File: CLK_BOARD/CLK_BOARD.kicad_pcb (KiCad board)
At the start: 4 copper layers, 73.6 x 37.4 mm, 83 parts, among them J1 PWR, J2 OUT_50M_1, J3 OUT_50M_2, J4 OUT_50M_3, J5 OUT_50M_4, J6 OUT_100M_3, J7 OUT_100M_2, J8 OUT_100M_1, J9 Conn_01x04, U1 TPS7A9101DSKR, U2 LMK00804BQWRGTRQ1, U3 LMK00804BQWRGTRQ1, U4 SN74LVC1G74DCUR, X1 TB612-100.0M

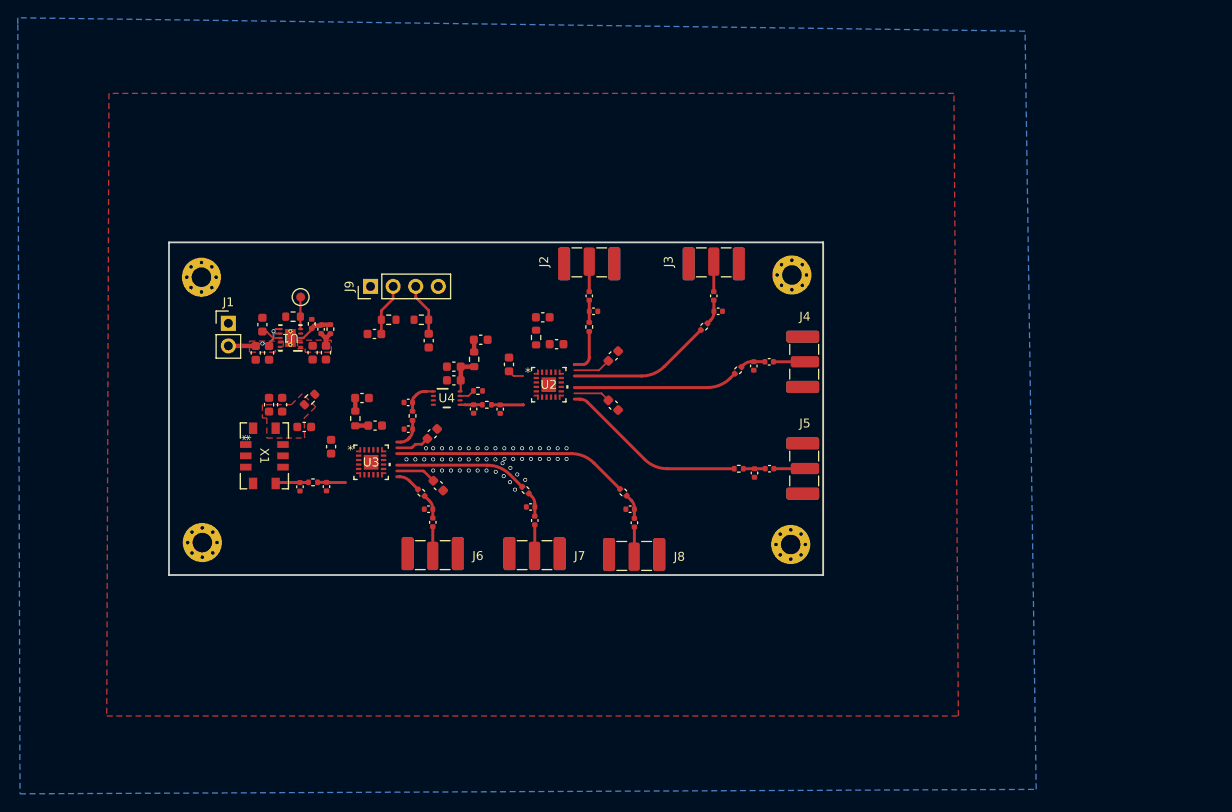
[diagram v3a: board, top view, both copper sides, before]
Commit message: redid layout with QFN package instead of TSOP
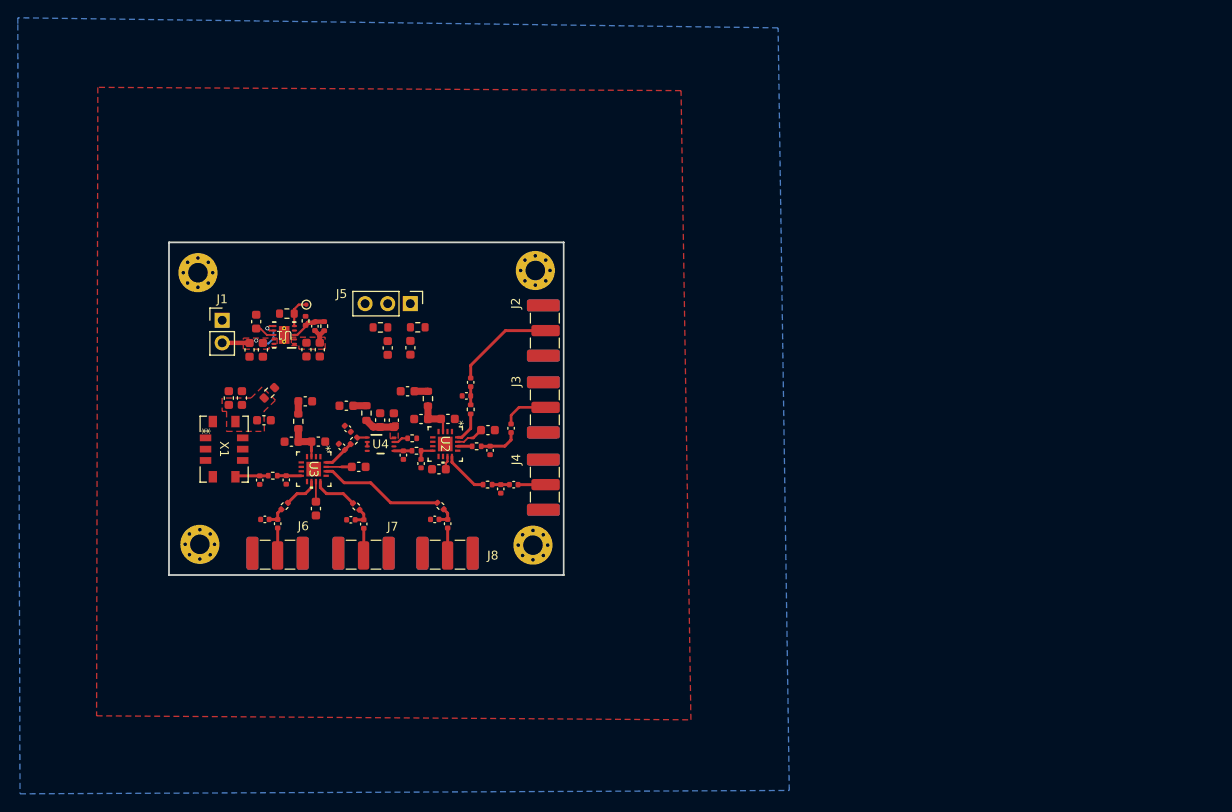
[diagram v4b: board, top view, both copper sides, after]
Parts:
- removed C30, C31: 10nF, Capacitor_SMD:C_0402_1005Metric
- removed J9: Conn_01x04, Connector_PinHeader_2.54mm:PinHeader_1x04_P2.54mm_Vertical
- removed R13: 43, Resistor_SMD:R_0402_1005Metric
- J5: value OUT_50M_4 -> CTRL; footprint Connector_Coaxial:SMA_Samtec_SMA-J-P-H-ST-EM1_EdgeMount -> Connector_PinHeader_2.54mm:PinHeader_1x03_P2.54mm_Vertical
- moved J5 48.1 mm to (101.4, 66.9), turned to -90 degrees
- moved J4 32.3 mm to (116.6, 87.2)
- moved C28 31.9 mm to (113.0, 87.2)
- moved C29 31.6 mm to (111.5, 87.7)
- moved R11 31.0 mm to (110.1, 87.2), turned to 0 degrees
- moved C23 30.0 mm to (110.3, 83.4), turned to -90 degrees
- moved H4 29.0 mm to (115.2, 94.0)
- moved R8 28.9 mm to (108.8, 82.9), turned to 0 degrees
- moved H2 28.8 mm to (115.4, 63.2)
- moved C22 27.2 mm to (112.7, 80.9)
- moved J3 25.0 mm to (116.6, 78.5), turned to 0 degrees
- moved C34 22.0 mm to (104.1, 91.2)
- moved C37 21.0 mm to (105.6, 91.6)
- moved J8 21.0 mm to (105.6, 95.2)
- moved R16 20.6 mm to (104.8, 89.6)
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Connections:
- J5 pad 1: Net-(J5-In) -> /nMUTE
- J5 pad 2: GND -> /nRST
- U2 pad 10: Net-(U2-Q3) -> unconnected-(U2-Q3-Pad10)
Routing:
- net Net-(U2-Q3): track 21.0 -> 0.00 mm
- net Net-(U2-Q1): track 16.2 -> 1.62 mm
- net Net-(U2-Q2): track 18.5 -> 5.18 mm
- net Net-(U3-Q1): track 26.6 -> 14.0 mm
- net Net-(U3-Q2): track 15.0 -> 5.08 mm
- net Net-(J2-In): track 3.38 -> 11.5 mm
- net /nRST: track 5.93 -> 0.00 mm
- net /nMUTE: track 5.90 -> 0.00 mm
- net Net-(J5-In): track 3.51 -> 0.00 mm
- net Net-(U4-CLK): track 4.02 -> 1.14 mm
- net Net-(C30-Pad2): track 2.47 -> 0.00 mm
- net Net-(J3-In): track 3.38 -> 5.23 mm
- net +3V3: track 6.04 -> 7.59 mm
- net Net-(U2-Q0): track 5.05 -> 3.50 mm
- net Net-(C22-Pad2): track 2.94 -> 4.49 mm
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- added copper zone on F.Cu, net Net-(U4-VCC)
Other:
- board size 73.6 x 37.4 mm -> 44.4 x 37.4 mm

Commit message: almost finished with layout
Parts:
- moved R16 10.1 mm to (95.0, 87.1), turned to 0 degrees
- moved C34 3.34 mm to (107.3, 90.2), turned to 0 degrees
- moved C37 1.29 mm to (106.9, 91.6)
- moved J8 1.29 mm to (106.9, 95.2)
- moved C32 1.07 mm to (84.0, 91.1)
- moved R14 1.07 mm to (86.2, 89.6)
- moved C35 1.07 mm to (85.4, 91.6)
- moved J6 1.07 mm to (85.4, 95.2)
- moved C9 0.82 mm to (110.2, 80.3), turned to 45 degrees
- moved H3 0.30 mm to (77.5, 94.2)
- moved R12 0.25 mm to (101.4, 81.9)
- moved H4 0.24 mm to (115.4, 94.2)
- moved C21 0.23 mm to (90.8, 90.2)
- moved H1 0.16 mm to (77.5, 63.2)
- moved H2 0.11 mm to (115.4, 63.2)
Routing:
- net +3V3: track 7.59 -> 59.7 mm, vias 0 -> 2
- net /nMUTE: track 0.00 -> 43.4 mm, vias 0 -> 3
- net /nRST: track 0.00 -> 19.0 mm, vias 0 -> 2
- net Net-(U3-VDD): track 9.78 -> 25.3 mm, vias 0 -> 3
- net Net-(U2-VDD): track 9.04 -> 22.2 mm, vias 0 -> 3
- net Net-(C34-Pad1): track 2.31 -> 13.7 mm
- net Net-(U3-Q1): track 14.0 -> 3.14 mm
- net Net-(U4-CLK): track 1.14 -> 2.12 mm
- net Net-(U3-Q3): track 4.04 -> 4.99 mm
- net GND: vias 0 -> 488
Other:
- board text added: "+4V"

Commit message: some fixes, some fixes to be done, not sure i love the layout
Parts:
- moved C32 3.87 mm to (87.2, 89.0), turned to -45 degrees
- moved C29 3.01 mm to (108.8, 86.5), turned to 45 degrees
- moved R11 2.97 mm to (107.4, 85.9), turned to -45 degrees
- moved R15 2.76 mm to (93.0, 88.2), turned to 0 degrees
- moved R14 2.76 mm to (88.5, 88.2), turned to 180 degrees
- moved C33 2.19 mm to (94.2, 89.0), turned to -135 degrees
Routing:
- net Net-(U2-Q2): track 5.13 -> 1.85 mm
- net Net-(C28-Pad2): track 1.95 -> 5.14 mm
- net Net-(U3-Q2): track 4.96 -> 2.07 mm
- net Net-(U3-Q3): track 4.99 -> 2.15 mm
- net Net-(C32-Pad1): track 2.22 -> 4.29 mm
- net Net-(C33-Pad1): track 2.26 -> 4.32 mm
- net +3V3: track 59.7 -> 60.5 mm
- net GND: vias 488 -> 474

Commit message: ported footprint changes to library, will be redoing the layout from the beginning because i was not happy with the result
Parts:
- J2, J3, J4, J6, J7, J8: footprint Connector_Coaxial:SMA_Samtec_SMA-J-P-H-ST-EM1_EdgeMount -> Snapeda:SMA_Samtec_SMA-J-P-H-ST-EM1_EdgeMount
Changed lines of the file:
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@@
 		)
 	)
-	(footprint "Connector_Coaxial:SMA_Samtec_SMA-J-P-H-ST-EM1_EdgeMount"
+	(footprint "Snapeda:SMA_Samtec_SMA-J-P-H-ST-EM1_EdgeMount"
 		(layer "F.Cu")
 		(at 106.865624 95.21 -90)
@@
 		)
 	)
-	(footprint "Connector_Coaxial:SMA_Samtec_SMA-J-P-H-ST-EM1_EdgeMount"
+	(footprint "Snapeda:SMA_Samtec_SMA-J-P-H-ST-EM1_EdgeMount"
 		(layer "F.Cu")
 		(at 96.125 95.2 -90)
@@
 		)
 	)
-	(footprint "Connector_Coaxial:SMA_Samtec_SMA-J-P-H-ST-EM1_EdgeMount"
+	(footprint "Snapeda:SMA_Samtec_SMA-J-P-H-ST-EM1_EdgeMount"
 		(layer "F.Cu")
 		(at 85.39 95.18 -90)
@@
 		)
 	)
-	(footprint "Connector_Coaxial:SMA_Samtec_SMA-J-P-H-ST-EM1_EdgeMount"
+	(footprint "Snapeda:SMA_Samtec_SMA-J-P-H-ST-EM1_EdgeMount"
 		(layer "F.Cu")
 		(at 116.59 78.55)
@@
 		)
 	)
-	(footprint "Connector_Coaxial:SMA_Samtec_SMA-J-P-H-ST-EM1_EdgeMount"
+	(footprint "Snapeda:SMA_Samtec_SMA-J-P-H-ST-EM1_EdgeMount"
 		(layer "F.Cu")
 		(at 116.59 87.24)
@@
 		(embedded_fonts no)
 	)
-	(footprint "Connector_Coaxial:SMA_Samtec_SMA-J-P-H-ST-EM1_EdgeMount"
+	(footprint "Snapeda:SMA_Samtec_SMA-J-P-H-ST-EM1_EdgeMount"
 		(layer "F.Cu")
 		(at 116.59 69.92)

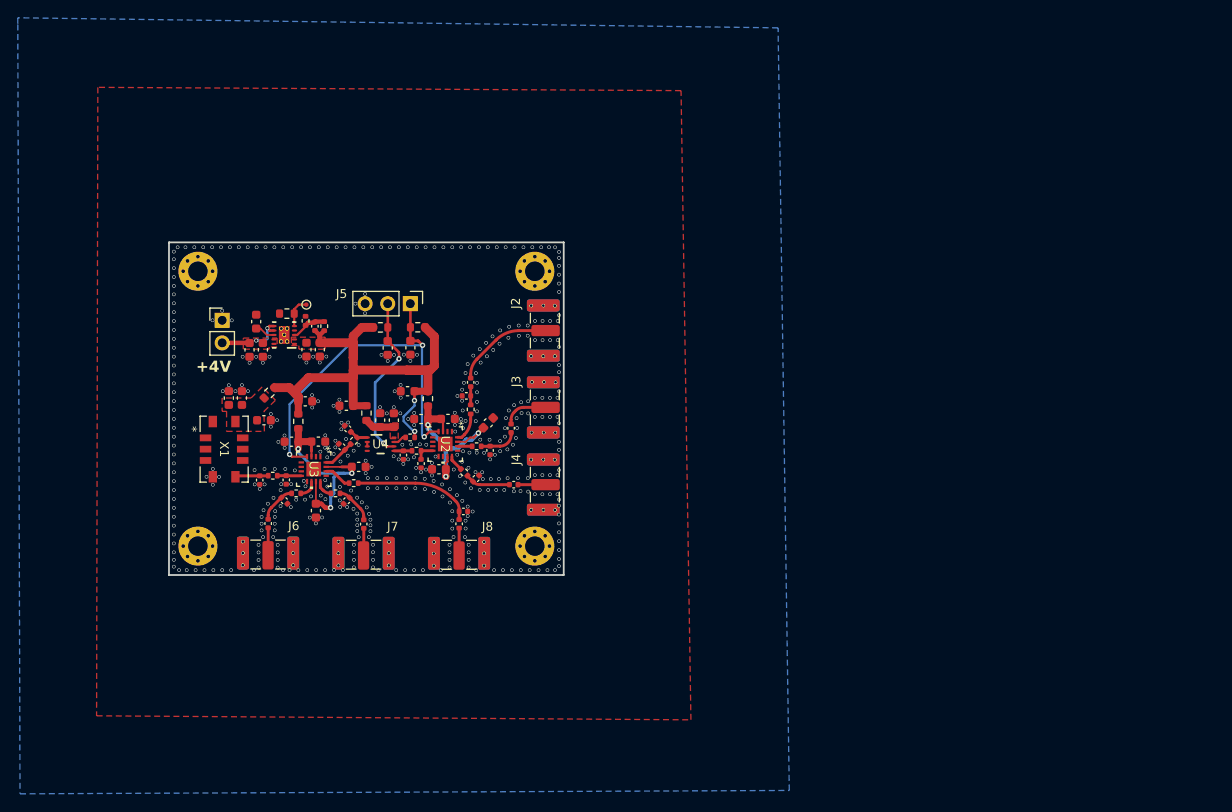
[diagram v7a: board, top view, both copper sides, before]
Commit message: restarted layout, first pass placement done
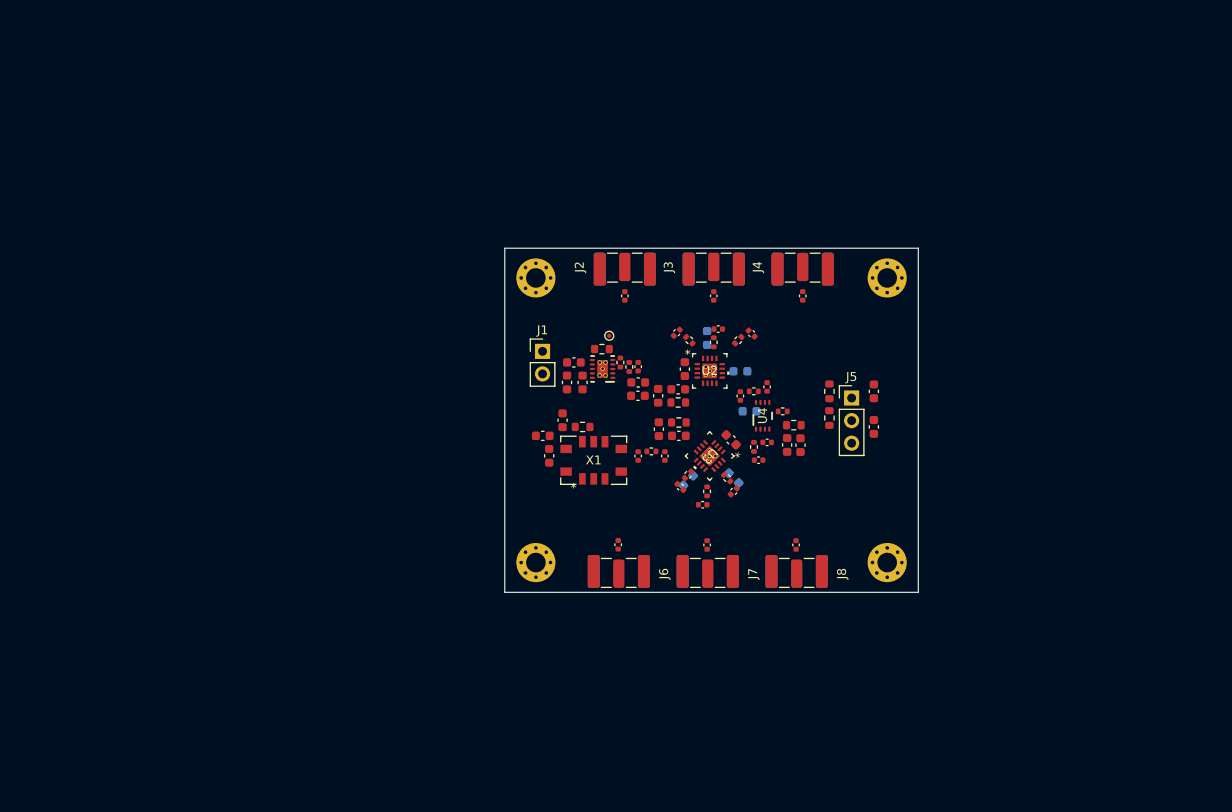
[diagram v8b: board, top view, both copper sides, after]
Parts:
- C10, C14, C19, C20, C9: moved to B.Cu
- moved H3 83.2 mm to (155.0, 64.0)
- moved C39 55.4 mm to (153.5, 80.8)
- moved C38 52.3 mm to (153.5, 76.8), turned to 90 degrees
- moved R18 51.5 mm to (148.5, 79.8), turned to 90 degrees
- moved C12 51.3 mm to (145.2, 82.8), turned to -90 degrees
- moved J5 50.7 mm to (151.0, 77.5), turned to 0 degrees
- moved R5 48.1 mm to (144.5, 80.5), turned to 180 degrees
- moved C21 47.4 mm to (137.5, 82.2), turned to -45 degrees
- moved C25 47.2 mm to (141.5, 82.5), turned to 0 degrees
- moved C19 46.9 mm to (137.8, 86.5), turned to -45 degrees
- moved C24 46.9 mm to (140.5, 84.5), turned to 0 degrees
- moved R17 46.8 mm to (148.5, 76.8), turned to -90 degrees
- moved C13 45.8 mm to (143.8, 82.8), turned to -90 degrees
- moved R9 45.0 mm to (140.0, 83.0), turned to 90 degrees
- moved C32 44.6 mm to (131.8, 87.5)
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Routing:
- net +3V3: track 60.5 -> 0.00 mm, vias 2 -> 0
- net /nMUTE: track 43.4 -> 0.00 mm, vias 3 -> 0
- net Net-(U3-VDD): track 25.7 -> 0.00 mm, vias 3 -> 0
- net Net-(U2-VDD): track 22.2 -> 0.00 mm, vias 3 -> 0
- net /nRST: track 19.0 -> 0.00 mm, vias 2 -> 0
- net Net-(C34-Pad1): track 13.7 -> 0.00 mm
- net Net-(J2-In): track 11.2 -> 0.00 mm
- net Net-(J1-Pin_2): track 7.29 -> 0.00 mm, vias 2 -> 0
- net Net-(C28-Pad2): track 5.14 -> 0.00 mm
- net Net-(J3-In): track 5.11 -> 0.00 mm
- net Net-(C33-Pad1): track 4.32 -> 0.00 mm
- net Net-(C22-Pad2): track 4.31 -> 0.00 mm
- net Net-(C32-Pad1): track 4.29 -> 0.00 mm
- net Net-(U1-FB): track 3.94 -> 0.00 mm
- net Net-(X1-OUTPUT): track 3.74 -> 0.00 mm
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- removed copper zone on F.Cu, net +3V3
- removed copper zone on B.Cu, net GND
- removed copper zone on F.Cu, net GND
- removed copper zone on In1.Cu, net GND
- removed copper zone on In2.Cu, net GND
- removed copper zone on F.Cu, net Net-(J1-Pin_2)
- removed copper zone on F.Cu, net Net-(U4-VCC)
- removed copper zone on F.Cu, net Net-(X1-VCC)
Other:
- board size 44.4 x 37.4 mm -> 46.5 x 38.7 mm
- board text removed: "+4V"
